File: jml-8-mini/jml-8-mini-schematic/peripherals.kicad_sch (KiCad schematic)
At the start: 8 parts, among them J2 SIO CHB, J3 UART, J4 CTC EXTRA LINES, U4 Z80 CTC, U5 Z80 SIO

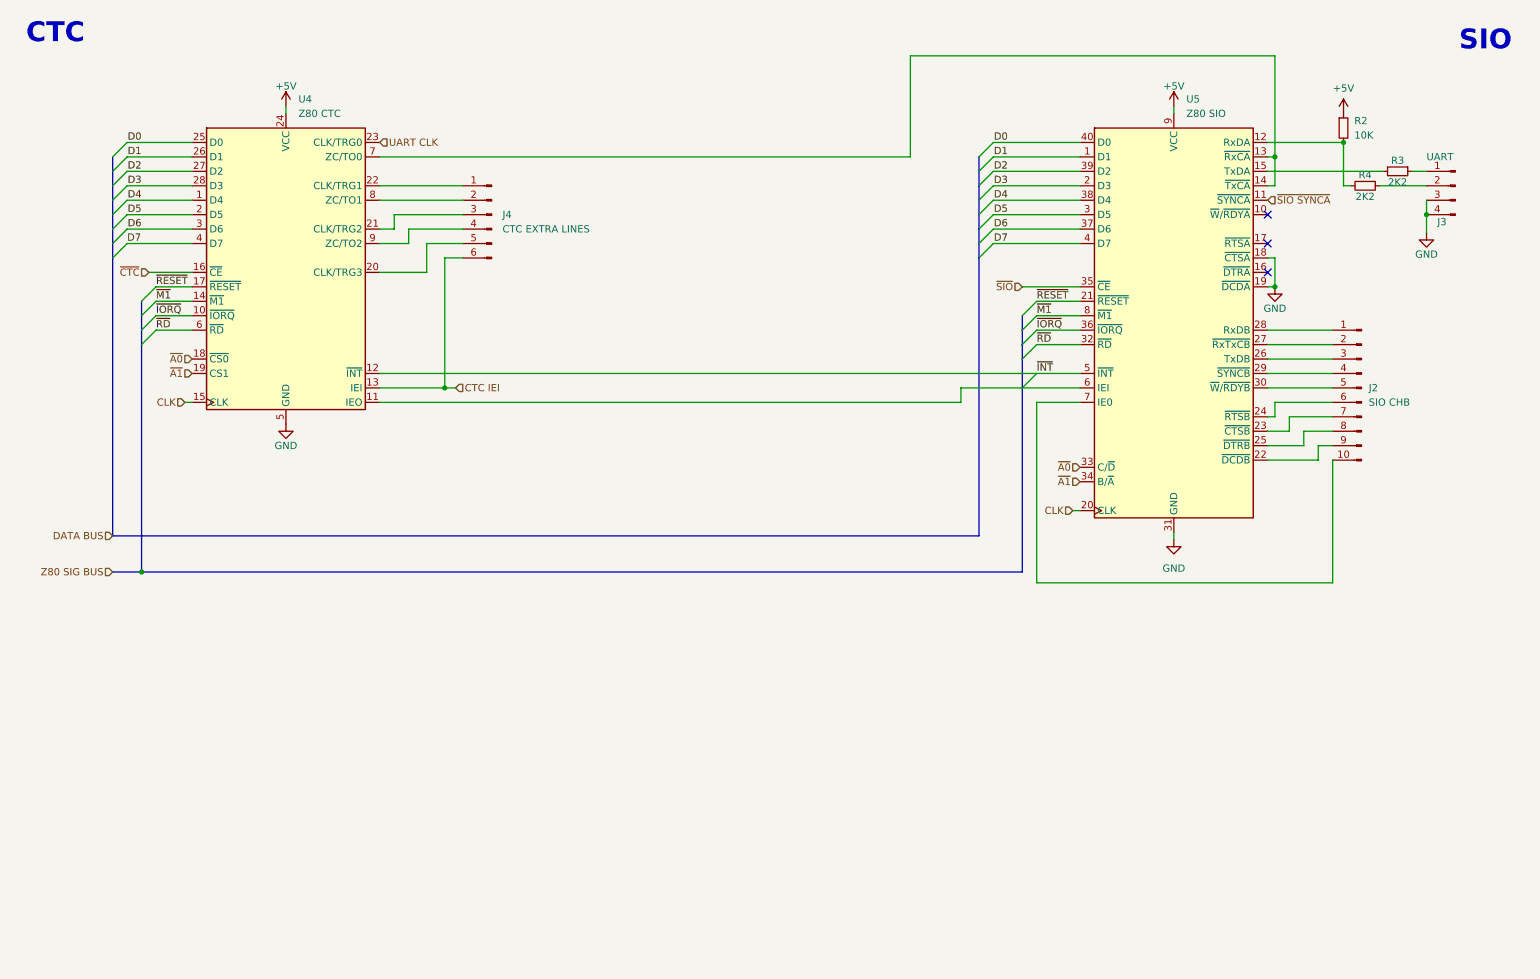
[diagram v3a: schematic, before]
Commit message: complete schematic
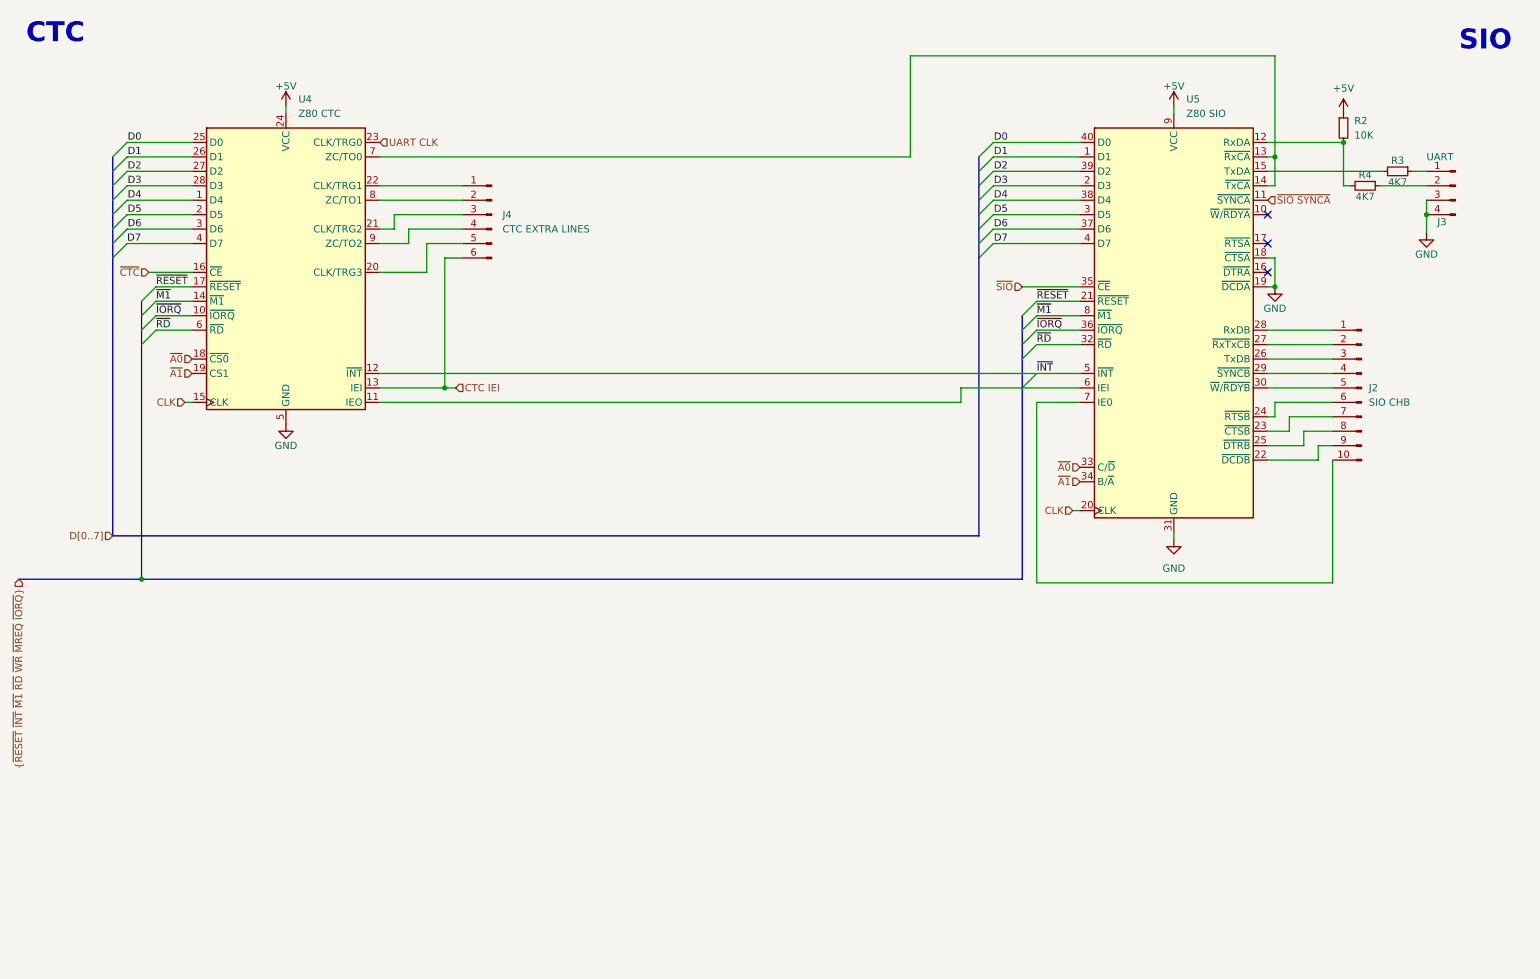
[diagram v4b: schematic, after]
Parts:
- J2: footprint (none) -> Connector_PinHeader_2.54mm:PinHeader_1x10_P2.54mm_Vertical
- J3: footprint (none) -> Connector_PinHeader_2.54mm:PinHeader_1x04_P2.54mm_Horizontal
- J4: footprint (none) -> Connector_PinHeader_2.54mm:PinHeader_1x06_P2.54mm_Vertical
- R2: footprint (none) -> Resistor_THT:R_Axial_DIN0207_L6.3mm_D2.5mm_P10.16mm_Horizontal
- R3, R4: value 2K2 -> 4K7; footprint (none) -> Resistor_THT:R_Axial_DIN0207_L6.3mm_D2.5mm_P10.16mm_Horizontal
- U4: footprint (none) -> Package_DIP:DIP-28_W15.24mm_LongPads
- U5: footprint (none) -> Package_DIP:DIP-40_W15.24mm_LongPads
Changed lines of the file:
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@@
 (kicad_sch (version 20230121) (generator eeschema)
   (paper "A4")
+  (title_block
+    (date "2023-10-02")
+    (rev "A")
+    (comment 1 "Author: Jacob Long")
+  )
   (junction (at 262.89 51.435) (diameter 0) (color 0 0 0 0)
   )
@@
   (junction (at 236.22 41.275) (diameter 0) (color 0 0 0 0)
   )
-  (junction (at 36.83 114.3) (diameter 0) (color 0 0 0 0)
-  )
   (junction (at 90.17 81.915) (diameter 0) (color 0 0 0 0)
   )
   (junction (at 236.22 64.135) (diameter 0) (color 0 0 0 0)
+  )
+  (junction (at 36.83 115.57) (diameter 0) (color 0 0 0 0)
   )
   (no_connect (at 234.95 61.595))
@@
     (stroke (width 0) (type default))
   )
-  (bus (pts (xy 36.83 114.3) (xy 36.83 74.295))
-    (stroke (width 0) (type default))
-  )
   (wire (pts (xy 201.93 43.815) (xy 186.69 43.815))
     (stroke (width 0) (type default))
@@
     (stroke (width 0) (type default))
   )
-  (bus (pts (xy 191.77 81.915) (xy 191.77 114.3))
+  (bus (pts (xy 191.77 81.915) (xy 191.77 115.57))
     (stroke (width 0) (type default))
   )
@@
     (stroke (width 0) (type default))
   )
+  (bus (pts (xy 36.83 74.295) (xy 36.83 115.57))
+    (stroke (width 0) (type default))
+  )
   (wire (pts (xy 234.95 38.735) (xy 248.285 38.735))
     (stroke (width 0) (type default))
@@
     (stroke (width 0) (type default))
   )
+  (bus (pts (xy 15.24 115.57) (xy 36.83 115.57))
+    (stroke (width 0) (type default))
+  )
   (wire (pts (xy 238.76 89.535) (xy 238.76 86.995))
     (stroke (width 0) (type default))
@@
     (stroke (width 0) (type default))
   )
+  (bus (pts (xy 36.83 115.57) (xy 191.77 115.57))
+    (stroke (width 0) (type default))
+  )
   (bus (pts (xy 31.75 53.975) (xy 31.75 56.515))
     (stroke (width 0) (type default))
@@
     (stroke (width 0) (type default))
   )
-  (bus (pts (xy 191.77 114.3) (xy 36.83 114.3))
-    (stroke (width 0) (type default))
-  )
   (wire (pts (xy 194.31 116.205) (xy 246.38 116.205))
     (stroke (width 0) (type default))
@@
   )
   (wire (pts (xy 78.74 56.515) (xy 83.82 56.515))
-    (stroke (width 0) (type default))
-  )
-  (bus (pts (xy 31.75 114.3) (xy 36.83 114.3))
     (stroke (width 0) (type default))
   )
@@
     (effects (font (size 1.27 1.27)) (justify left bottom))
   )
-  (hierarchical_label "Z80 SIG BUS" (shape input) (at 31.75 114.3 180) (fields_autoplaced)
+  (hierarchical_label "{~{RESET} ~{INT} ~{M1} ~{RD} ~{WR} ~{MREQ} ~{IORQ}}" (shape input)
+    (at 15.24 115.57 270) (fields_autoplaced)
     (effects (font (size 1.27 1.27)) (justify right))
   )
@@
     (effects (font (size 1.27 1.27)) (justify right))
   )
-  (hierarchical_label "DATA BUS" (shape input) (at 31.75 107.95 180) (fields_autoplaced)
+  (hierarchical_label "D[0..7]" (shape input) (at 31.75 107.95 180) (fields_autoplaced)
     (effects (font (size 1.27 1.27)) (justify right))
   )
@@
       (effects (font (size 1.27 1.27)))
     )
-    (property "Value" "2K2" (at 252.095 48.26 90)
+    (property "Value" "4K7" (at 252.095 48.26 90)
       (effects (font (size 1.27 1.27)))
     )
-    (property "Footprint" "" (at 252.095 46.355 0)
+    (property "Footprint" "Resistor_THT:R_Axial_DIN0207_L6.3mm_D2.5mm_P10.16mm_Horizontal" (at 252.095 46.355 0)
       (effects (font (size 1.27 1.27)) hide)
     )
@@
       (effects (font (size 1.27 1.27)) (justify right))
     )
-    (property "Footprint" "" (at 98.425 51.435 0)
+    (property "Footprint" "Connector_PinHeader_2.54mm:PinHeader_1x06_P2.54mm_Vertical" (at 98.425 51.435 0)
       (effects (font (size 1.27 1.27)) hide)
     )
@@
       (effects (font (size 1.27 1.27)) (justify left))
     )
-    (property "Footprint" "" (at 248.285 36.195 0)
+    (property "Footprint" "Resistor_THT:R_Axial_DIN0207_L6.3mm_D2.5mm_P10.16mm_Horizontal" (at 248.285 36.195 0)
       (effects (font (size 1.27 1.27)) hide)
     )
@@
       (effects (font (size 1.27 1.27)))
     )
-    (property "Value" "2K2" (at 257.81 45.72 90)
+    (property "Value" "4K7" (at 257.81 45.72 90)
       (effects (font (size 1.27 1.27)))
     )
-    (property "Footprint" "" (at 257.81 43.815 0)
+    (property "Footprint" "Resistor_THT:R_Axial_DIN0207_L6.3mm_D2.5mm_P10.16mm_Horizontal" (at 257.81 43.815 0)
       (effects (font (size 1.27 1.27)) hide)
     )
@@
       (effects (font (size 1.27 1.27)) (justify right))
     )
-    (property "Footprint" "" (at 251.46 81.915 0)
+    (property "Footprint" "Connector_PinHeader_2.54mm:PinHeader_1x10_P2.54mm_Vertical" (at 251.46 81.915 0)
       (effects (font (size 1.27 1.27)) hide)
     )
@@
       (effects (font (size 1.27 1.27)) (justify right))
     )
-    (property "Footprint" "" (at 267.97 46.355 0)
+    (property "Footprint" "Connector_PinHeader_2.54mm:PinHeader_1x04_P2.54mm_Horizontal" (at 267.97 46.355 0)
       (effects (font (size 1.27 1.27)) hide)
     )
@@
       (effects (font (size 1.27 1.27)) (justify left))
     )
-    (property "Footprint" "" (at 224.79 81.915 0)
+    (property "Footprint" "Package_DIP:DIP-40_W15.24mm_LongPads" (at 224.79 81.915 0)
       (effects (font (size 1.27 1.27)) hide)
     )
@@
       (effects (font (size 1.27 1.27)) (justify left))
     )
-    (property "Footprint" "" (at 62.23 59.055 0)
-      (effects (font (size 1.27 1.27)) hide)
-    )
+    (property "Footprint" "Package_DIP:DIP-28_W15.24mm_LongPads" (at 62.23 59.055 0)
+      (effects (font (size 1.27 1.27)) hide)
+    )

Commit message: add to info section of schematic
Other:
- company: (none) -> https://github.com/jac-oblong/jml
- title: (none) -> JML-8 Mini Schematic
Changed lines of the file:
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@@
   (paper "A4")
   (title_block
+    (title "JML-8 Mini Schematic")
     (date "2023-10-02")
     (rev "A")
-    (comment 1 "Author: Jacob Long")
+    (company "https://github.com/jac-oblong/jml")
+    (comment 1 "Design of Z80 based microcomputer")
+    (comment 3 "Released under MIT License")
+    (comment 4 "Created by: Jacob Long (https://github.com/jac-oblong)")
   )
   (junction (at 262.89 51.435) (diameter 0) (color 0 0 0 0)
